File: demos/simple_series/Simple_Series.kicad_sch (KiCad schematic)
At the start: 3 parts, among them SW1 SPST

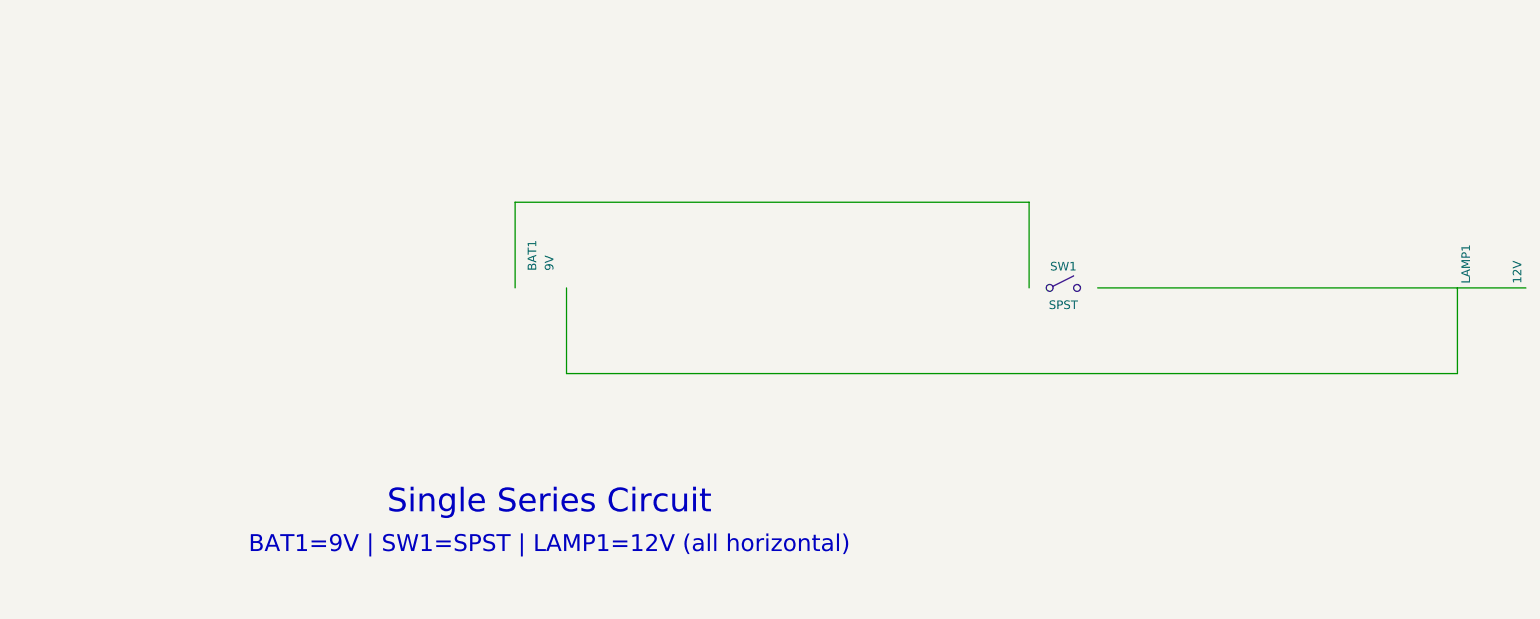
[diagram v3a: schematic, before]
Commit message: feat: add SPICE simulation module and related tests
- Implemented a new SPICE simulation module in `spice.py` that exports KiCad schematics to SPICE netlists and runs simulations using ngspice.
- Added preprocessing for netlists to handle power placeholders and GND mappings.
- Created tests for drawing an RC circuit, probing simulation symbols, and running SPICE simulations.
- Verified the integration of the `kicad_sch_simulate` tool within the MCP session.
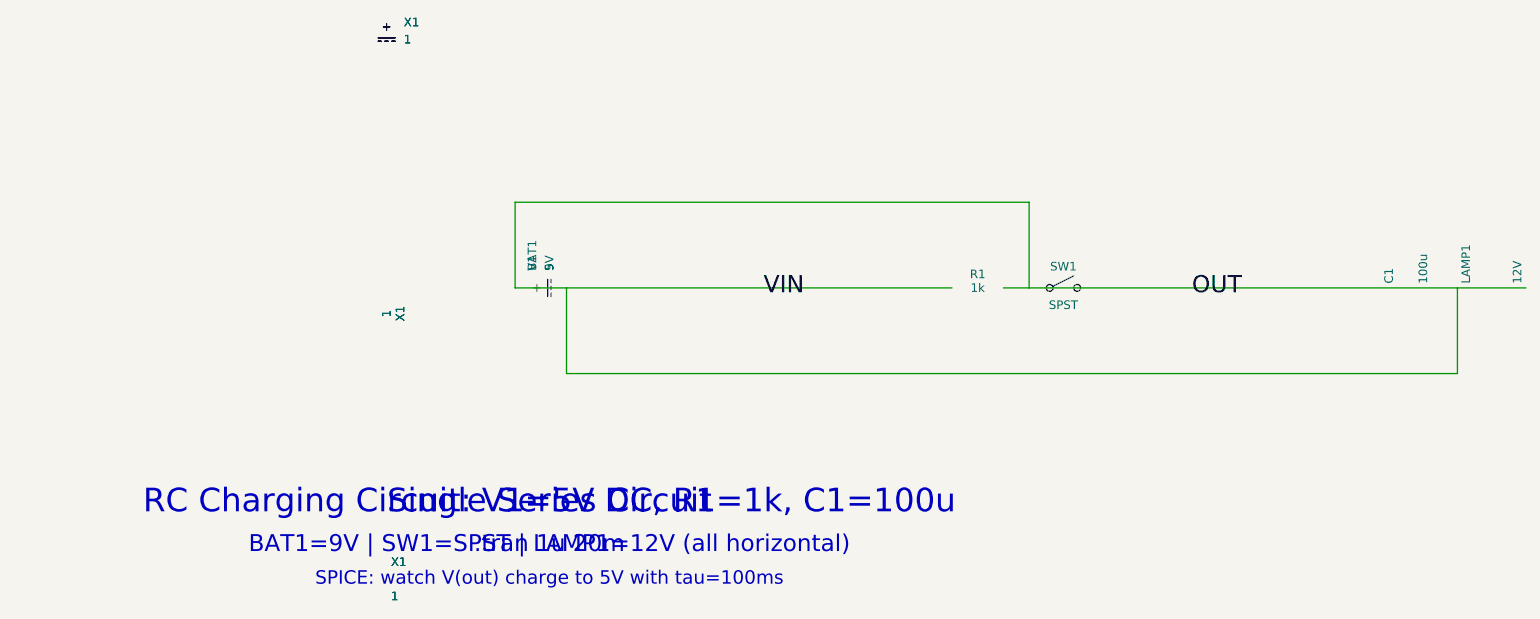
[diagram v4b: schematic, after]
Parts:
- added C1: 100u, symbol Device:C
- added R1: 1k, symbol Device:R
- added V1: 5, symbol Simulation_SPICE:VDC
- added X1 (x2): 1, symbol Device:C
- added X1 (x2): 1, symbol Device:R
- added X1 (x2): 1, symbol Simulation_SPICE:VDC
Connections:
- net at SW1.2 (B): no longer LAMP1.1 (-)
- net VIN: now reaches BAT1.1 (+), SW1.1 (A)
- net VIN: now also R1.1, V1.1
- new net: X1.1, X1.1 (x3)
- new net: X1.2, X1.2 (x3)
- new net OUT: LAMP1.1 (-), R1.2
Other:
- note added: ".tran 1u 20m"
- note added: "RC Charging Circuit: V1=5V DC, R1=1k, C1=100u"
- note added: "SPICE: watch V(out) charge to 5V with tau=100ms"
